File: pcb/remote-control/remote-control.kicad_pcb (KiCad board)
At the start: 2 copper layers, 20 x 20 mm, 12 parts, among them IC1 ATTINY44-S, P1 Bat+, P3 Bat-, Q1 Q_NMOS_GSD, T1 TEST

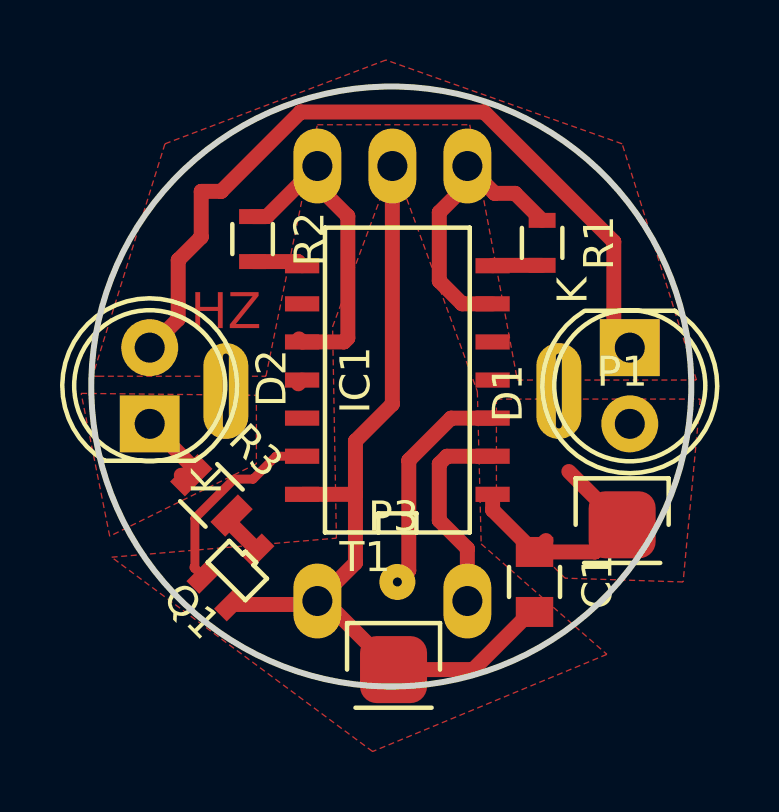
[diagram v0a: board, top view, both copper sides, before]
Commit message: o Make IR engergy storage 1206 SMD size o add 0603 package for 100n bypass.
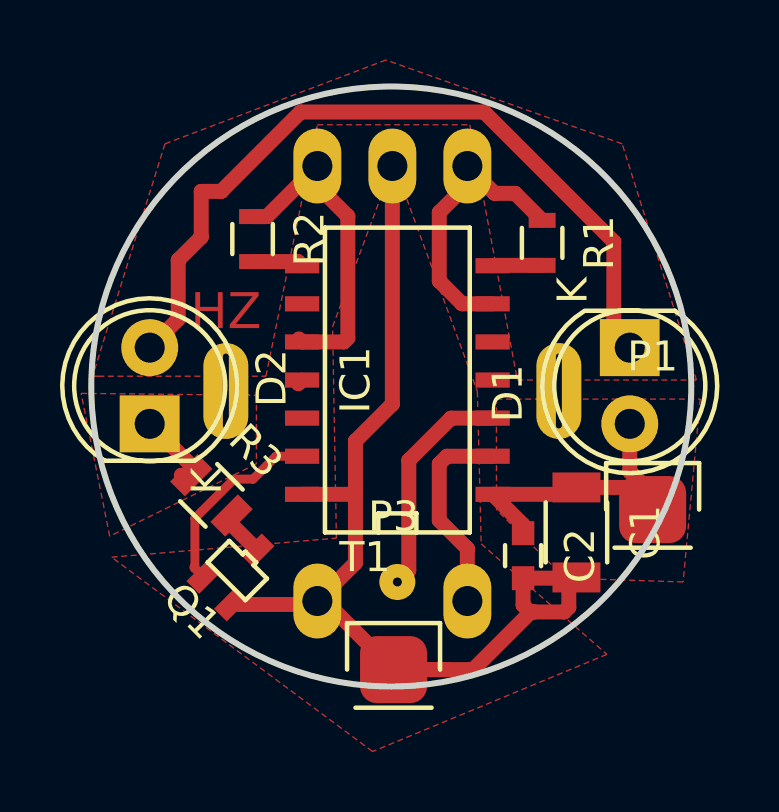
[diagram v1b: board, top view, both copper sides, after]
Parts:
- added C2: 100n, Capacitors_SMD:C_0603, F.Cu at (104.4, 55.6)
- C1: value 10u -> 22u; footprint Capacitors_SMD:C_0805 -> Capacitors_SMD:C_1206
- moved C1 2.16 mm to (106.2, 54.9)
- moved P1 1.14 mm to (108.7, 54.1)
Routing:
- net GND: track 29.3 -> 36.5 mm
- net VCC: track 9.94 -> 11.3 mm
